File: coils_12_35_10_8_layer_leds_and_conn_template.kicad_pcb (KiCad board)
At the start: 8 copper layers, 20 x 20 mm, 61 parts

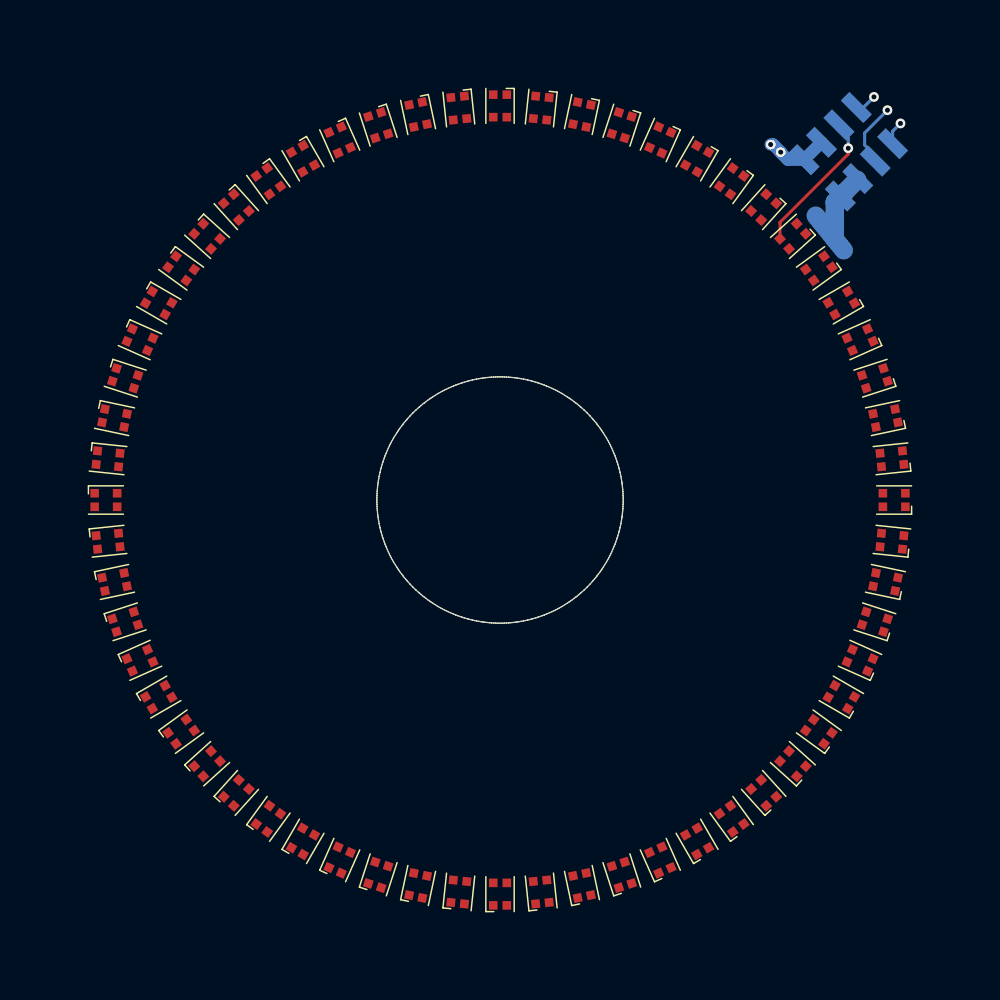
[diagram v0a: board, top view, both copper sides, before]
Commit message: Corrected PCB template
board outline was on wrong layer
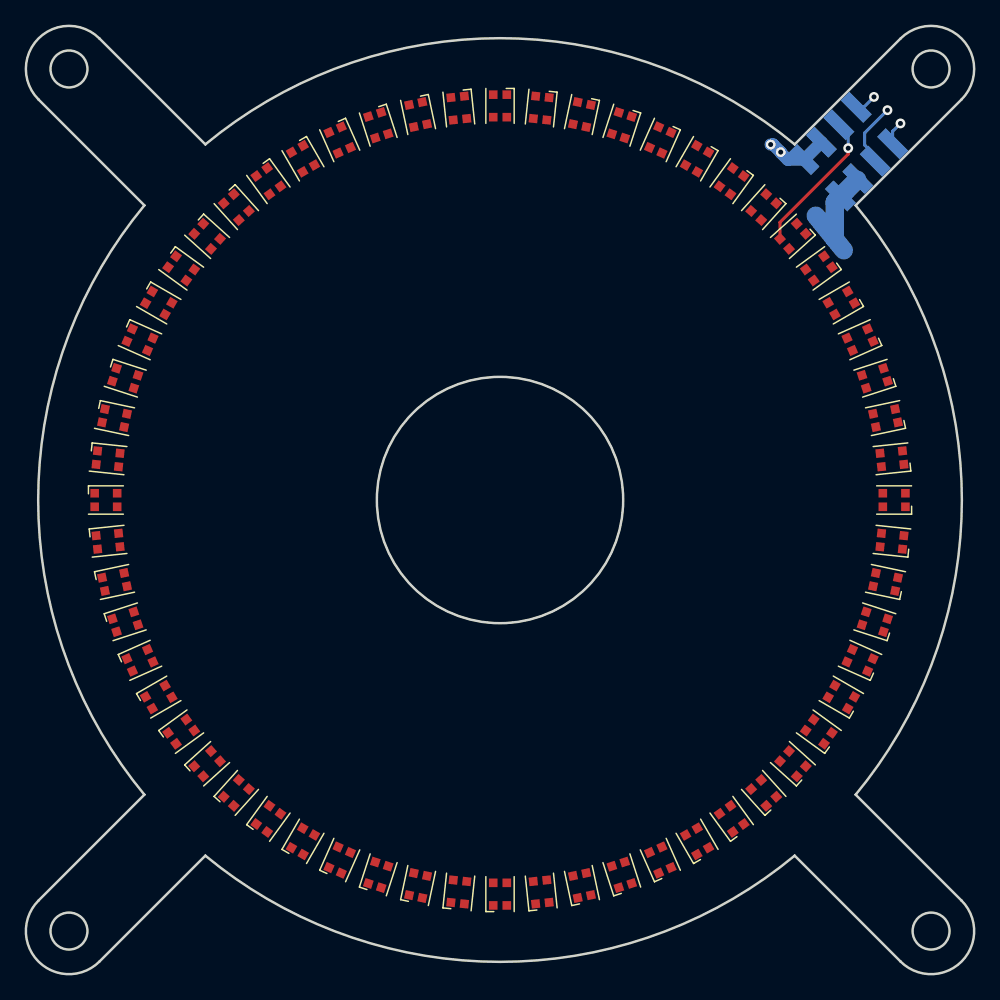
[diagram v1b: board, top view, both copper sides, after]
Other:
- board size 20 x 20 mm -> 77 x 77 mm
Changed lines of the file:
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@@
       (xy 160 100)
     ) (layer "F.Mask") (width 0.1) (fill none))
-  (gr_arc (start 187.474874 132.525126) (mid 187.474874 137.474874) (end 182.525126 137.474874) (layer "Dwgs.User") (width 0.2))
-  (gr_line (start 178.875631 76.074116) (end 187.474874 67.474874) (layer "Dwgs.User") (width 0.2))
-  (gr_arc (start 182.525126 62.525126) (mid 187.474874 62.525126) (end 187.474874 67.474874) (layer "Dwgs.User") (width 0.2))
-  (gr_line (start 182.525126 62.525126) (end 173.925884 71.124369) (layer "Dwgs.User") (width 0.2))
-  (gr_arc (start 112.525126 67.474874) (mid 112.525126 62.525126) (end 117.474874 62.525126) (layer "Dwgs.User") (width 0.2))
-  (gr_circle (center 185 65) (end 186.5 65) (layer "Dwgs.User") (width 0.2) (fill none))
-  (gr_line (start 112.525126 67.474874) (end 121.124369 76.074116) (layer "Dwgs.User") (width 0.2))
-  (gr_arc (start 173.925884 128.875631) (mid 150 137.5) (end 126.074116 128.875631) (layer "Dwgs.User") (width 0.2))
-  (gr_line (start 187.474874 132.525126) (end 178.875631 123.925884) (layer "Dwgs.User") (width 0.2))
-  (gr_circle (center 150 100) (end 160 100) (layer "Dwgs.User") (width 0.2) (fill none))
-  (gr_line (start 121.124369 123.925884) (end 112.525126 132.525126) (layer "Dwgs.User") (width 0.2))
-  (gr_circle (center 115 65) (end 116.5 65) (layer "Dwgs.User") (width 0.2) (fill none))
-  (gr_arc (start 121.124369 123.925884) (mid 112.5 100) (end 121.124369 76.074116) (layer "Dwgs.User") (width 0.2))
-  (gr_line (start 126.074116 71.124369) (end 117.474874 62.525126) (layer "Dwgs.User") (width 0.2))
-  (gr_arc (start 178.875631 76.074116) (mid 187.5 100) (end 178.875631 123.925884) (layer "Dwgs.User") (width 0.2))
-  (gr_circle (center 115 135) (end 116.5 135) (layer "Dwgs.User") (width 0.2) (fill none))
-  (gr_arc (start 126.074116 71.124369) (mid 150 62.5) (end 173.925884 71.124369) (layer "Dwgs.User") (width 0.2))
-  (gr_arc (start 117.474874 137.474874) (mid 112.525126 137.474874) (end 112.525126 132.525126) (layer "Dwgs.User") (width 0.2))
-  (gr_circle (center 185 135) (end 186.5 135) (layer "Dwgs.User") (width 0.2) (fill none))
-  (gr_line (start 173.925884 128.875631) (end 182.525126 137.474874) (layer "Dwgs.User") (width 0.2))
-  (gr_line (start 117.474874 137.474874) (end 126.074116 128.875631) (layer "Dwgs.User") (width 0.2))
+  (gr_line (start 178.875631 76.074116) (end 187.474874 67.474874) (layer "Edge.Cuts") (width 0.2))
+  (gr_line (start 187.474874 132.525126) (end 178.875631 123.925884) (layer "Edge.Cuts") (width 0.2))
+  (gr_arc (start 173.925884 128.875631) (mid 150 137.5) (end 126.074116 128.875631) (layer "Edge.Cuts") (width 0.2))
   (gr_poly
     (pts
@@
       (xy 160 100)
     ) (layer "Edge.Cuts") (width 0.1) (fill none))
+  (gr_circle (center 115 65) (end 116.5 65) (layer "Edge.Cuts") (width 0.2) (fill none))
+  (gr_circle (center 115 135) (end 116.5 135) (layer "Edge.Cuts") (width 0.2) (fill none))
+  (gr_arc (start 182.525126 62.525126) (mid 187.474874 62.525126) (end 187.474874 67.474874) (layer "Edge.Cuts") (width 0.2))
+  (gr_arc (start 178.875631 76.074116) (mid 187.5 100) (end 178.875631 123.925884) (layer "Edge.Cuts") (width 0.2))
+  (gr_arc (start 187.474874 132.525126) (mid 187.474874 137.474874) (end 182.525126 137.474874) (layer "Edge.Cuts") (width 0.2))
+  (gr_line (start 182.525126 62.525126) (end 173.925884 71.124369) (layer "Edge.Cuts") (width 0.2))
+  (gr_line (start 117.474874 137.474874) (end 126.074116 128.875631) (layer "Edge.Cuts") (width 0.2))
+  (gr_arc (start 112.525126 67.474874) (mid 112.525126 62.525126) (end 117.474874 62.525126) (layer "Edge.Cuts") (width 0.2))
+  (gr_arc (start 126.074116 71.124369) (mid 150 62.5) (end 173.925884 71.124369) (layer "Edge.Cuts") (width 0.2))
+  (gr_arc (start 117.474874 137.474874) (mid 112.525126 137.474874) (end 112.525126 132.525126) (layer "Edge.Cuts") (width 0.2))
+  (gr_line (start 121.124369 123.925884) (end 112.525126 132.525126) (layer "Edge.Cuts") (width 0.2))
+  (gr_arc (start 121.124369 123.925884) (mid 112.5 100) (end 121.124369 76.074116) (layer "Edge.Cuts") (width 0.2))
+  (gr_circle (center 185 135) (end 186.5 135) (layer "Edge.Cuts") (width 0.2) (fill none))
+  (gr_line (start 173.925884 128.875631) (end 182.525126 137.474874) (layer "Edge.Cuts") (width 0.2))
+  (gr_line (start 126.074116 71.124369) (end 117.474874 62.525126) (layer "Edge.Cuts") (width 0.2))
+  (gr_circle (center 150 100) (end 160 100) (layer "Edge.Cuts") (width 0.2) (fill none))
+  (gr_line (start 112.525126 67.474874) (end 121.124369 76.074116) (layer "Edge.Cuts") (width 0.2))
+  (gr_circle (center 185 65) (end 186.5 65) (layer "Edge.Cuts") (width 0.2) (fill none))
   (via (at 181.459125 68.345445) (size 0.8) (drill 0.4) (layers "F.Cu" "B.Cu") (free) (net 1))
   (via (at 182.515088 69.421331) (size 0.8) (drill 0.4) (layers "F.Cu" "B.Cu") (free) (net 1))
@@
   (segment (start 178 70) (end 178.271315 70.271315) (width 0.25) (layer "B.Cu") (net 4))
   (segment (start 177.982213 70) (end 178 70) (width 0.25) (layer "B.Cu") (net 4))
-  (group "" (id 7c8099d1-44b5-4271-af63-eda02cbfb6be)
+  (group "" (id 6bf52ec1-cf28-4985-9509-67a57e72e580)
     (members
-      00ec47e2-95e0-4256-9102-6b807fc46125
-      0271871e-5c17-4ef0-a7b0-368d2b5801d5
-      0ff31a57-280f-47fd-b851-36a31ad9f43f
-      1648a839-1043-4771-ae30-82cd69ed5b2b
-      172a9418-fe54-4b15-b690-ccded40f1140
-      1799d948-c42a-483f-8ac7-b8a5f2283c3c
-      2180eb54-2102-44a5-a44a-92cd03a56091
-      24ad2a77-4ebb-4522-858f-0b166b6b7821
-      2d39f36d-545b-45aa-9c1f-6317de2e6b57
-      3bda874a-5ba9-4499-b15a-8483d19b640f
-      3e261825-ad72-42a7-9642-3273fd168c69
-      56d5eecf-9f42-4e46-a66c-05854b06a8af
-      65556ca8-e413-44fc-82e6-28c75217c826
-      67310a1b-f822-4e3e-971f-f9f1135a2875
-      7e619f08-09f2-4278-9beb-6d824d312cbc
-      7eb5f061-4d9d-42aa-9ce2-4c36f4fa119d
-      8075c62c-a76b-475b-bead-ce13cfaa8cd7
-      aa1fd0af-2149-4362-a7c8-08e4e7ae2d69
-      cdafaedd-89bb-4836-8a13-0af26e95abab
-      db3ff299-5d81-4489-b22b-4c556e0b9afa
-      fa67dcba-aa2d-42c3-8d1a-fff8ff4fbba7
+      15cbd655-605b-4e6b-9880-35234a935fde
+      1b3d2cfd-9649-4db4-b4c4-baa61ffafe1e
+      34abf0ba-6d8b-4061-a037-b000cd7b90b7
+      403771e2-d845-4ad7-9872-b630c584228e
+      458ec1c0-da27-446a-b07d-e67839ea78ce
+      4a1d5ac5-a6fc-4824-9185-496da9c0d0b7
+      5b79cc88-9862-4a52-a871-996e9e8bcf43
+      781d06ce-67e9-461c-8c78-b12fed9e8ce8
+      7b2d6db4-f3eb-4e37-83ae-b2abe77bfbf8
+      7c1adb20-f4fc-4b5e-9635-4dcc8022a7cc
+      828a2353-1bb7-410b-bfc5-be8b620325c6
+      839815bf-384a-4d26-886d-1fa6224a64e7
+      8abb75f1-9715-4021-a59c-7987f70b7b90
+      8ae88554-00d8-40c1-ae07-afb10de99149
+      a5a873fb-b0e5-4cc0-a8f1-5c2743f57eed
+      ae0cbf59-5d73-4a35-8aed-0e2d40a3b5b8
+      ce0849e4-cb4d-44fc-904b-f6bb4ab6ac9a
+      db36c845-4996-475d-94ca-3251f90036c3
+      e935aa2e-dafa-4127-b05d-89eedb200056
+      f52b6157-2139-4869-b8ff-370d3ff5403f
+      f56604cc-aa89-4fbd-abd0-dd7d56e02fe0
     )
   )
